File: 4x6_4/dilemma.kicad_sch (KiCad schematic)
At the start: 349 parts, among them J1 USB_C_Receptacle_USB2.0, J102 NA_serial, J105 NA_Conn_01x04_Female, J113 Cirque, J3 NA_GC9A01, J4 Conn_01x05, J5 NA_Conn_01x02, J5001 USB_C_Receptacle_USB2.0, J5002 NA_Conn_01x02, J5003 NA_serial, J5004 NA_GC9A01, J5005 NA_Conn_01x04_Female, J5007 Cirque, J5008 Conn_01x05, J5009 Conn_01x05, J5010 Conn_01x05, SW1 SW_Push, SW101 NA_SW_Push, SW102 NA_SW_Push, SW103 NA_SW_Push, SW104 NA_SW_Push, SW105 NA_SW_Push, SW106 NA_SW_Push, SW107 NA_SW_Push, SW108 NA_SW_Push, SW109 NA_SW_Push, SW112 NA_SW_Push, SW113 NA_SW_Push, SW114 NA_SW_Push, SW115 NA_SW_Push, SW116 NA_SW_Push, SW117 NA_SW_Push, SW118 NA_SW_Push, SW119 NA_SW_Push, SW3001 NA_SW_Push, SW3002 NA_RotaryEncoder_Switch, SW5001 SW_Push, SW5002 NA_SW_Push, SW5003 NA_SW_Push, SW5004 NA_SW_Push, SW5005 NA_SW_Push, SW5006 NA_SW_Push, SW5007 NA_SW_Push, SW5008 NA_SW_Push, SW5009 NA_SW_Push, SW5010 NA_SW_Push, SW5011 NA_SW_Push, SW5012 NA_SW_Push, SW5013 NA_SW_Push, SW5014 NA_SW_Push, SW5015 NA_SW_Push, SW5016 NA_SW_Push, SW5017 NA_SW_Push, SW5018 NA_SW_Push, SW5019 NA_SW_Push, SW5020 NA_RotaryEncoder_Switch, SW5021 SW_SPST, SW5022 SW_SPST, SW5023 NA_SW_Push, SW5024 NA_SW_Push, SW5025 NA_SW_Push, SW5026 NA_SW_Push, SW5027 NA_SW_Push, SW5028 NA_SW_Push, SW5029 NA_SW_Push, SW5030 NA_SW_Push, SW5031 NA_SW_Push, SW5032 NA_SW_Push, SW5033 NA_SW_Push, SW5034 NA_SW_Push, SW5035 NA_SW_Push, SW5036 NA_SW_Push, SW5037 NA_SW_Push, SW5038 NA_SW_Push, SW5039 NA_SW_Push, SW5040 NA_SW_Push, SW5041 NA_SW_Push, SW5042 NA_SW_Push, U1 RP2040, U2 W25Q128JVS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

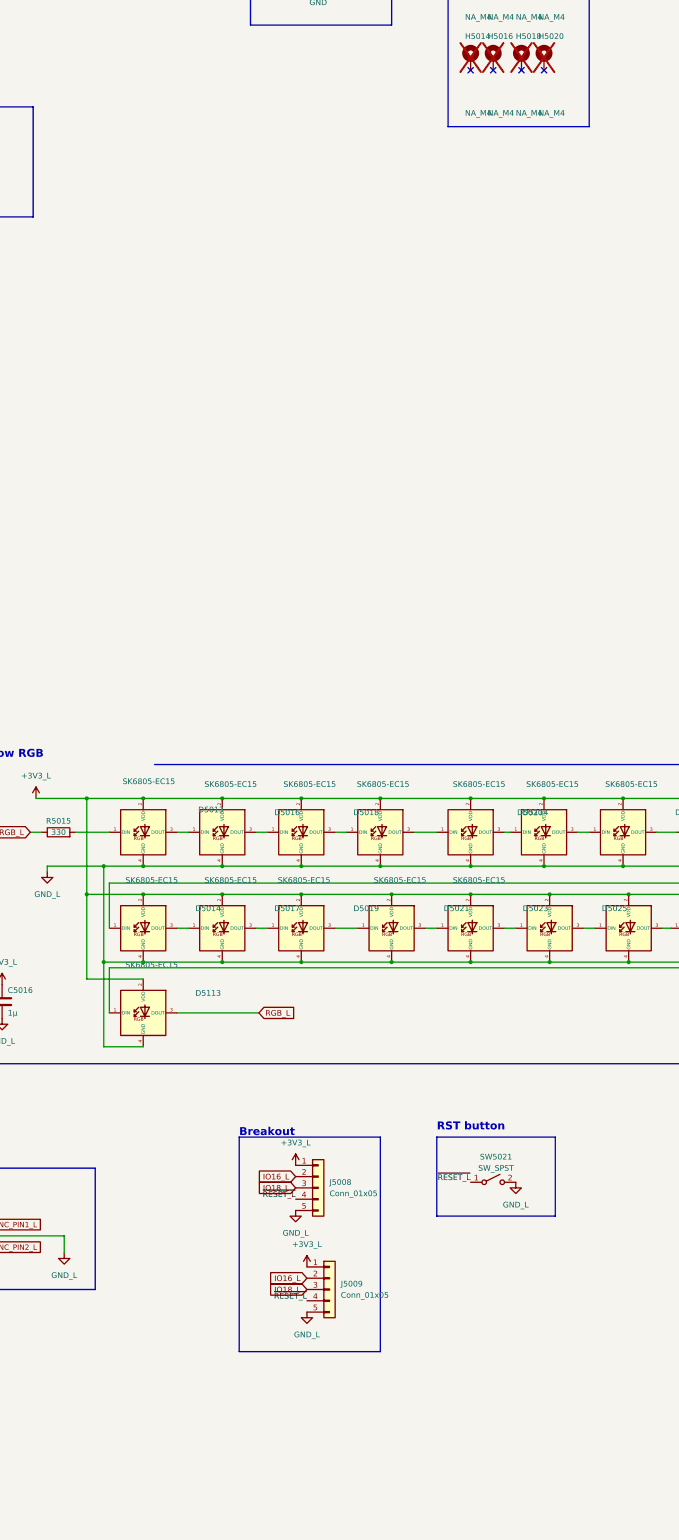
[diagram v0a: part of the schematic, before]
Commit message: move io header
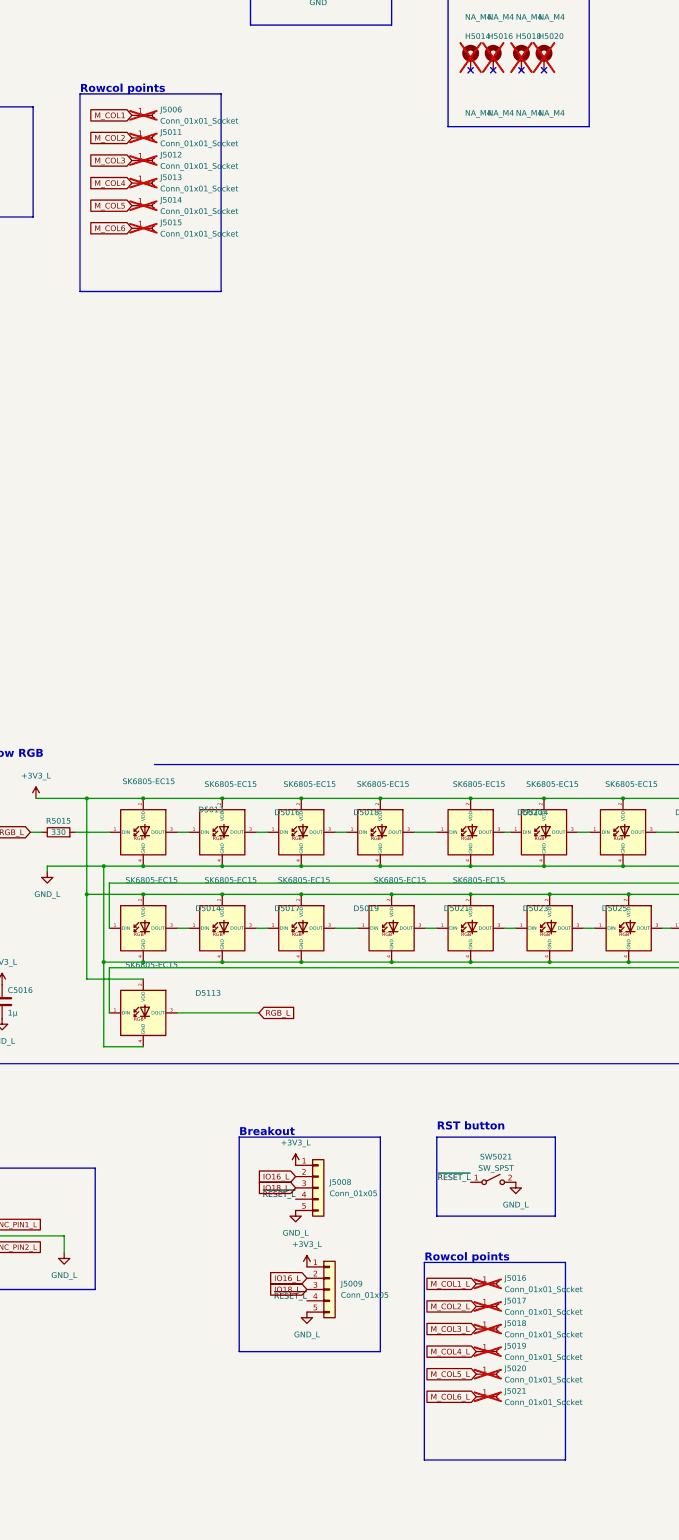
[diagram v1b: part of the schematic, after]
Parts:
- added J5006, J5011, J5012, J5013, J5014, J5015, J5016, J5017, J5018, J5019, J5020, J5021: Conn_01x01_Socket, local-libraries:testpoint, symbol Connector:Conn_01x01_Socket
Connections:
- net M_COL1: now also J5006.1 (Pin_1)
- net M_COL1_L: now also J5016.1 (Pin_1)
- net M_COL2: now also J5011.1 (Pin_1)
- net M_COL2_L: now also J5017.1 (Pin_1)
- net M_COL3: now also J5012.1 (Pin_1)
- net M_COL3_L: now also J5018.1 (Pin_1)
- net M_COL4: now also J5013.1 (Pin_1)
- net M_COL4_L: now also J5019.1 (Pin_1)
- net M_COL5: now also J5014.1 (Pin_1)
- net M_COL5_L: now also J5020.1 (Pin_1)
- net M_COL6: now also J5015.1 (Pin_1)
- net M_COL6_L: now also J5021.1 (Pin_1)
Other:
- note added: "Rowcol points"
